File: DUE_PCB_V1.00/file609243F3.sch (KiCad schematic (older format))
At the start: 13 parts, among them J26 Cutter, J27 MotorR, J28 MotorL, J32 24V In, U1 MC33926, U2 MC33926

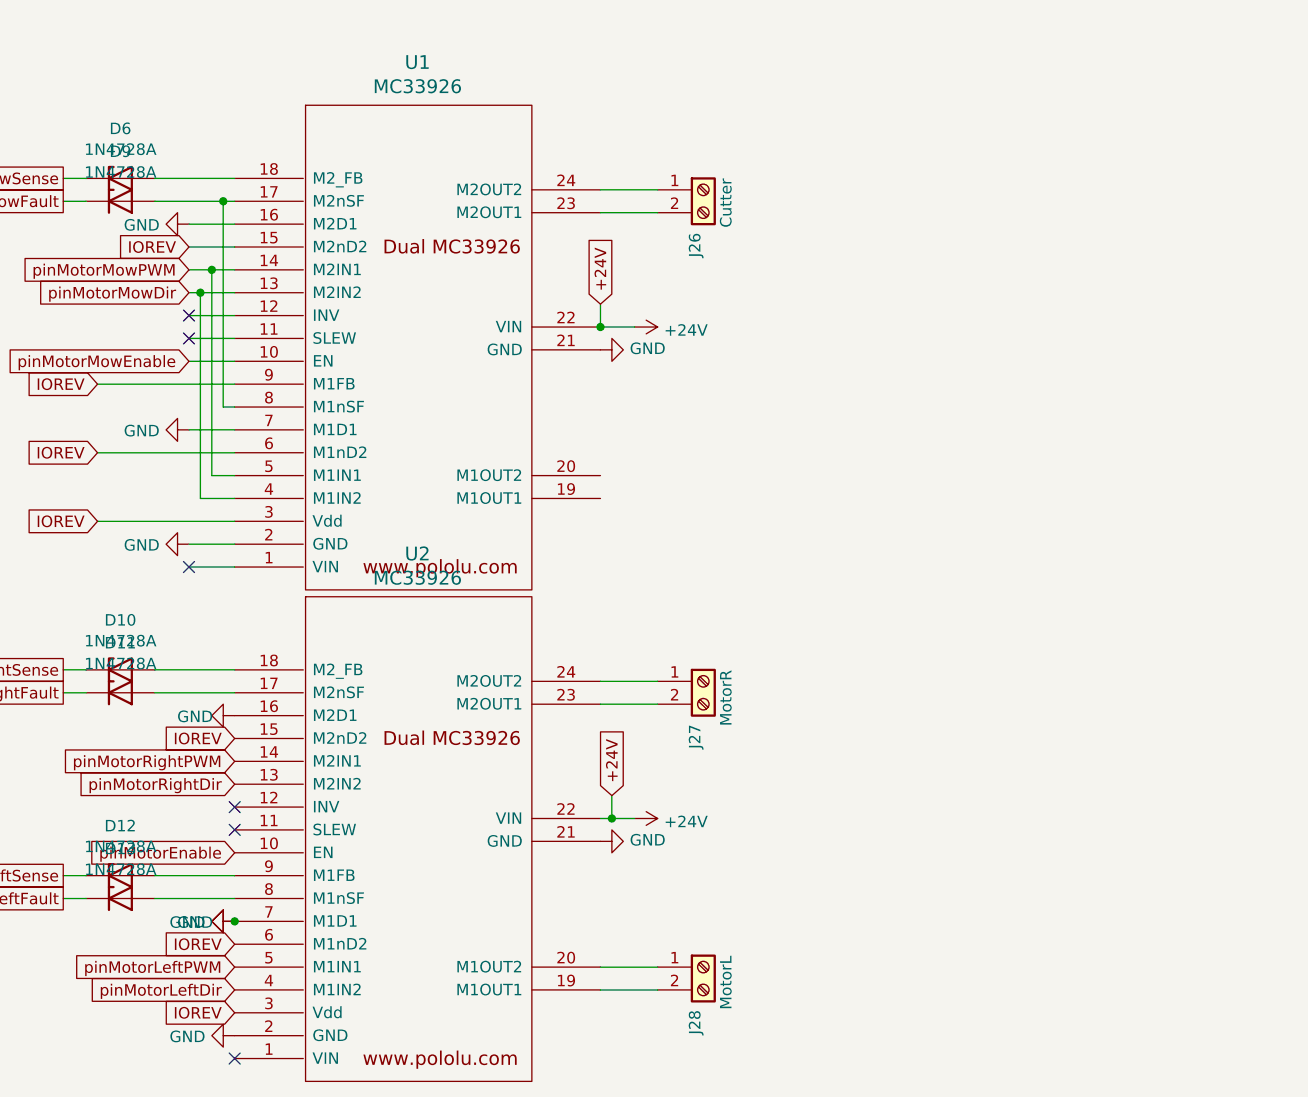
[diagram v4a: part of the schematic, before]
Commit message: Ad Odometrie Connector without Voltage Divider
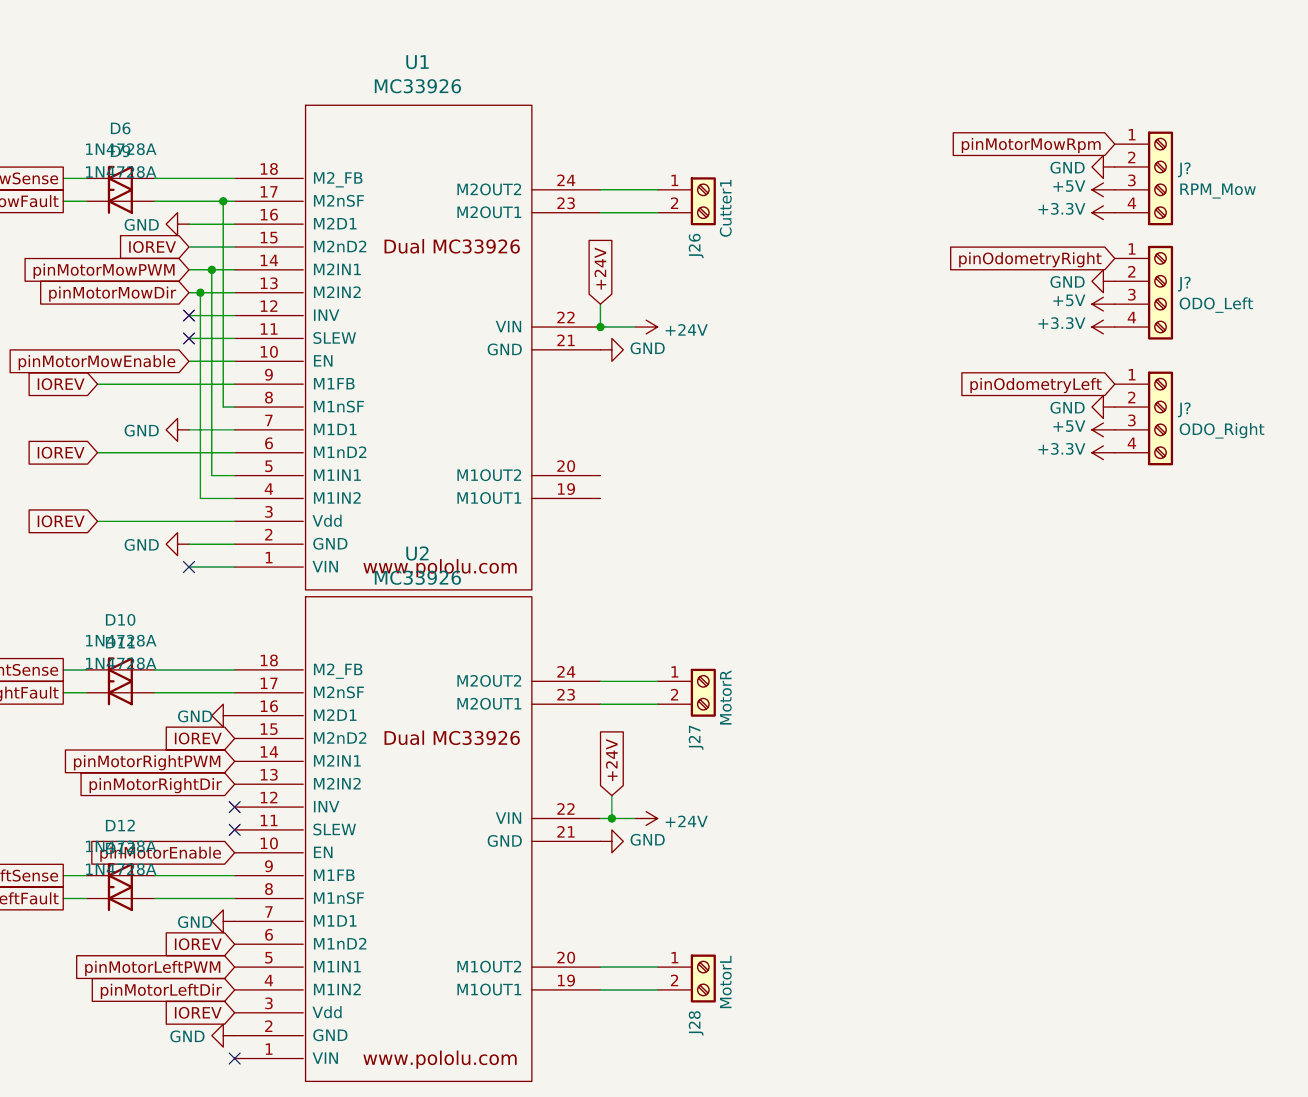
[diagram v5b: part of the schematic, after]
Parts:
- added J?: RPM_Mow, symbol Connector:Screw_Terminal_01x04
- added J?: ODO_Left, symbol Connector:Screw_Terminal_01x04
- added J?: ODO_Right, symbol Connector:Screw_Terminal_01x04
- J26: value Cutter -> Cutter1
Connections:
- net GND: now also J?.2 (Pin_2), J?.2 (Pin_2), J?.2 (Pin_2)
- new net +3V3: J?.4 (Pin_4), J?.4 (Pin_4), J?.4 (Pin_4)
- new net +5V: J?.3 (Pin_3), J?.3 (Pin_3), J?.3 (Pin_3)
- new net pinMotorMowRpm: J?.1 (Pin_1)
- new net pinOdometryLeft: J?.1 (Pin_1)
- new net pinOdometryRight: J?.1 (Pin_1)
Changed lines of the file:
@@
-$Comp
-L power:GND #PWR?
-U 1 1 60958CA1
-P 4300 4550
-AR Path="/60958CA1" Ref="#PWR?"  Part="1"
-AR Path="/609243F4/60958CA1" Ref="#PWR057"  Part="1"
-F 0 "#PWR057" H 4300 4300 50  0001 C CNN
-F 1 "GND" V 4305 4422 50  0000 R CNN
-F 2 "" H 4300 4550 50  0001 C CNN
-F 3 "" H 4300 4550 50  0001 C CNN
-	1    4300 4550
-	0    1    1    0
-$EndComp
 $Comp
 L power:GND #PWR?
@@
 P 6350 1350
 F 0 "J26" V 6314 1162 50  0000 R CNN
-F 1 "Cutter" V 6450 1400 50  0000 R CNN
+F 1 "Cutter1" V 6450 1400 50  0000 R CNN
 F 2 "TerminalBlock:TerminalBlock_bornier-2_P5.08mm" H 6350 1350 50  0001 C CNN
 F 3 "~" H 6350 1350 50  0001 C CNN
@@
 Wire Wire Line
 	3950 4450 4300 4450
-Connection ~ 4300 4550
+$Comp
+L Connector:Screw_Terminal_01x04 J?
+U 1 1 609ECE3C
+P 8350 1250
+F 0 "J?" H 8430 1242 50  0000 L CNN
+F 1 "RPM_Mow" H 8430 1151 50  0000 L CNN
+F 2 "" H 8350 1250 50  0001 C CNN
+F 3 "~" H 8350 1250 50  0001 C CNN
+	1    8350 1250
+	1    0    0    -1
+$EndComp
+$Comp
+L power:+3.3V #PWR?
+U 1 1 609FEF3C
+P 8150 1450
+F 0 "#PWR?" H 8150 1300 50  0001 C CNN
+F 1 "+3.3V" V 8165 1578 50  0000 L CNN
+F 2 "" H 8150 1450 50  0001 C CNN
+F 3 "" H 8150 1450 50  0001 C CNN
+	1    8150 1450
+	0    -1   -1   0
+$EndComp
+$Comp
+L power:+5V #PWR?
+U 1 1 60A02069
+P 8150 1350
+F 0 "#PWR?" H 8150 1200 50  0001 C CNN
+F 1 "+5V" V 8165 1478 50  0000 L CNN
+F 2 "" H 8150 1350 50  0001 C CNN
+F 3 "" H 8150 1350 50  0001 C CNN
+	1    8150 1350
+	0    -1   -1   0
+$EndComp
+$Comp
+L power:GND #PWR?
+U 1 1 60A04DCE
+P 8150 1250
+F 0 "#PWR?" H 8150 1000 50  0001 C CNN
+F 1 "GND" V 8155 1122 50  0000 R CNN
+F 2 "" H 8150 1250 50  0001 C CNN
+F 3 "" H 8150 1250 50  0001 C CNN
+	1    8150 1250
+	0    1    1    0
+$EndComp
+Text GLabel 8150 1150 0    50   Input ~ 0
+pinMotorMowRpm
+$Comp
+L Connector:Screw_Terminal_01x04 J?
+U 1 1 60A0AEEA
+P 8350 1750
+F 0 "J?" H 8430 1742 50  0000 L CNN
+F 1 "ODO_Left" H 8430 1651 50  0000 L CNN
+F 2 "" H 8350 1750 50  0001 C CNN
+F 3 "~" H 8350 1750 50  0001 C CNN
+	1    8350 1750
+	1    0    0    -1
+$EndComp
+$Comp
+L power:+3.3V #PWR?
+U 1 1 60A0B19C
+P 8150 1950
+F 0 "#PWR?" H 8150 1800 50  0001 C CNN
+F 1 "+3.3V" V 8165 2078 50  0000 L CNN
+F 2 "" H 8150 1950 50  0001 C CNN
+F 3 "" H 8150 1950 50  0001 C CNN
+	1    8150 1950
+	0    -1   -1   0
+$EndComp
+$Comp
+L power:+5V #PWR?
+U 1 1 60A0B1A6
+P 8150 1850
+F 0 "#PWR?" H 8150 1700 50  0001 C CNN
+F 1 "+5V" V 8165 1978 50  0000 L CNN
+F 2 "" H 8150 1850 50  0001 C CNN
+F 3 "" H 8150 1850 50  0001 C CNN
+	1    8150 1850
+	0    -1   -1   0
+$EndComp
+$Comp
+L power:GND #PWR?
+U 1 1 60A0B1B0
+P 8150 1750
+F 0 "#PWR?" H 8150 1500 50  0001 C CNN
+F 1 "GND" V 8155 1622 50  0000 R CNN
+F 2 "" H 8150 1750 50  0001 C CNN
+F 3 "" H 8150 1750 50  0001 C CNN
+	1    8150 1750
+	0    1    1    0
+$EndComp
+Text GLabel 8150 1650 0    50   Input ~ 0
+pinOdometryRight
+$Comp
+L Connector:Screw_Terminal_01x04 J?
+U 1 1 60A0D0C7
+P 8350 2300
+F 0 "J?" H 8430 2292 50  0000 L CNN
+F 1 "ODO_Right" H 8430 2201 50  0000 L CNN
+F 2 "" H 8350 2300 50  0001 C CNN
+F 3 "~" H 8350 2300 50  0001 C CNN
+	1    8350 2300
+	1    0    0    -1
+$EndComp
+$Comp
+L power:+3.3V #PWR?
+U 1 1 60A0D3D3
+P 8150 2500
+F 0 "#PWR?" H 8150 2350 50  0001 C CNN
+F 1 "+3.3V" V 8165 2628 50  0000 L CNN
+F 2 "" H 8150 2500 50  0001 C CNN
+F 3 "" H 8150 2500 50  0001 C CNN
+	1    8150 2500
+	0    -1   -1   0
+$EndComp
+$Comp
+L power:+5V #PWR?
+U 1 1 60A0D3DD
+P 8150 2400
+F 0 "#PWR?" H 8150 2250 50  0001 C CNN
+F 1 "+5V" V 8165 2528 50  0000 L CNN
+F 2 "" H 8150 2400 50  0001 C CNN
+F 3 "" H 8150 2400 50  0001 C CNN
+	1    8150 2400
+	0    -1   -1   0
+$EndComp
+$Comp
+L power:GND #PWR?
+U 1 1 60A0D3E7
+P 8150 2300
+F 0 "#PWR?" H 8150 2050 50  0001 C CNN
+F 1 "GND" V 8155 2172 50  0000 R CNN
+F 2 "" H 8150 2300 50  0001 C CNN
+F 3 "" H 8150 2300 50  0001 C CNN
+	1    8150 2300
+	0    1    1    0
+$EndComp
+Text GLabel 8150 2200 0    50   Input ~ 0
+pinOdometryLeft
 $EndSCHEMATC

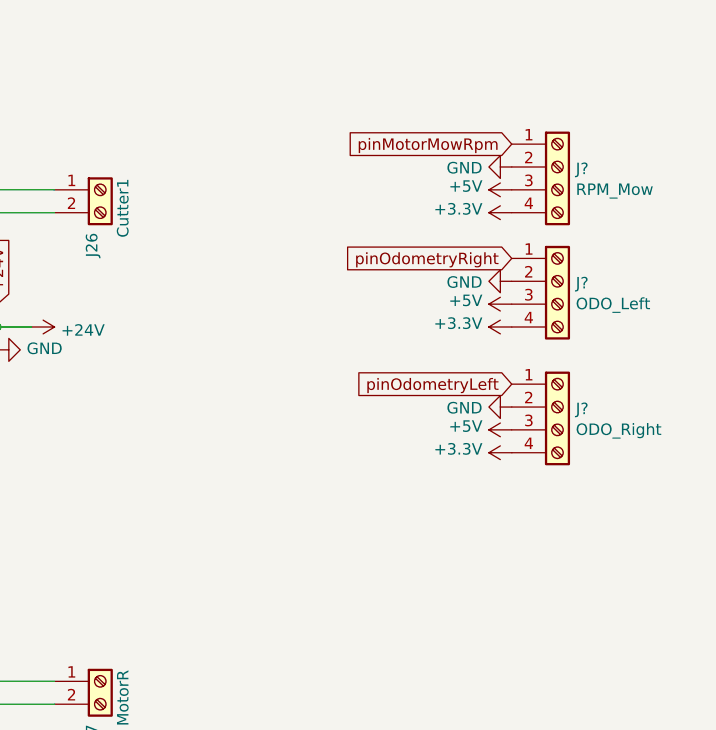
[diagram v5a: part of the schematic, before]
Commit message: Add Voltage Divider to ODO
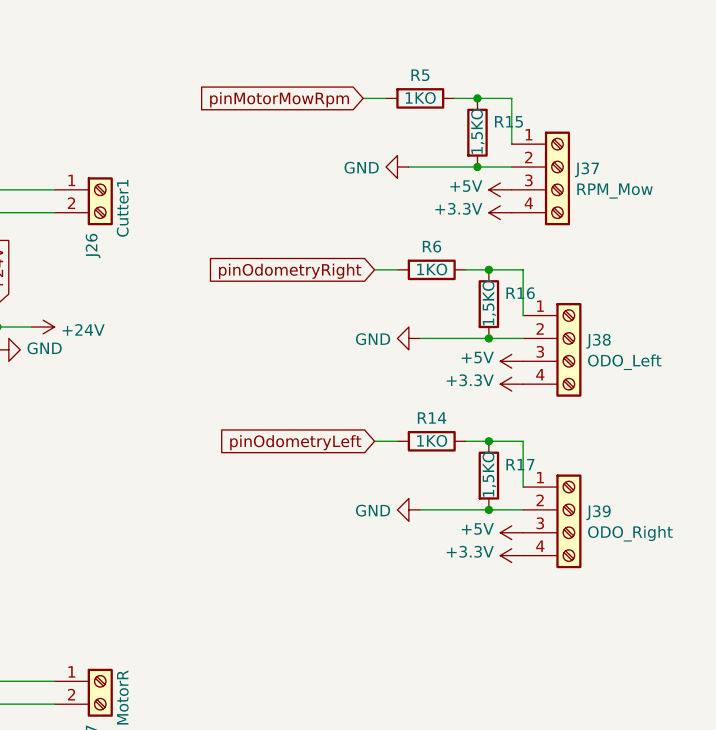
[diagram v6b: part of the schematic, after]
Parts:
- added R14, R5, R6: 1KO, Resistor_THT:R_Axial_DIN0207_L6.3mm_D2.5mm_P2.54mm_Vertical, symbol Device:R
- added R15, R16, R17: 1,5KO, Resistor_THT:R_Axial_DIN0207_L6.3mm_D2.5mm_P2.54mm_Vertical, symbol Device:R
- J37, J38, J39: renamed from J?; footprint (none) -> Connector_PinHeader_2.54mm:PinHeader_1x04_P2.54mm_Vertical
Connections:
- net GND: now also R15.2, R16.2, R17.2
- net pinMotorMowRpm: now also R5.2; no longer J37.1 (Pin_1)
- net pinOdometryLeft: now also R14.2; no longer J39.1 (Pin_1)
- net pinOdometryRight: now also R6.2; no longer J38.1 (Pin_1)
- new net: J37.1 (Pin_1), R15.1, R5.1
- new net: J38.1 (Pin_1), R16.1, R6.1
- new net: J39.1 (Pin_1), R14.1, R17.1
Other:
- moved on the sheet: J38, J39

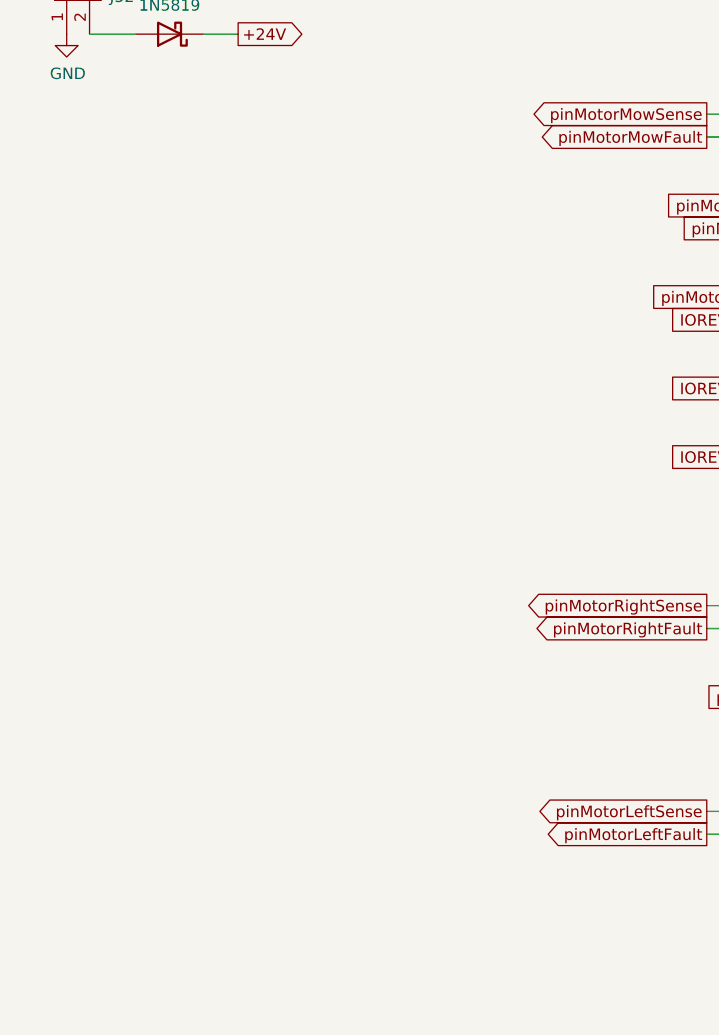
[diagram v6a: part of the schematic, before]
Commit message: Add Motor Connectors
Add Default Motor Connectors and reorder Ser0-Ser3
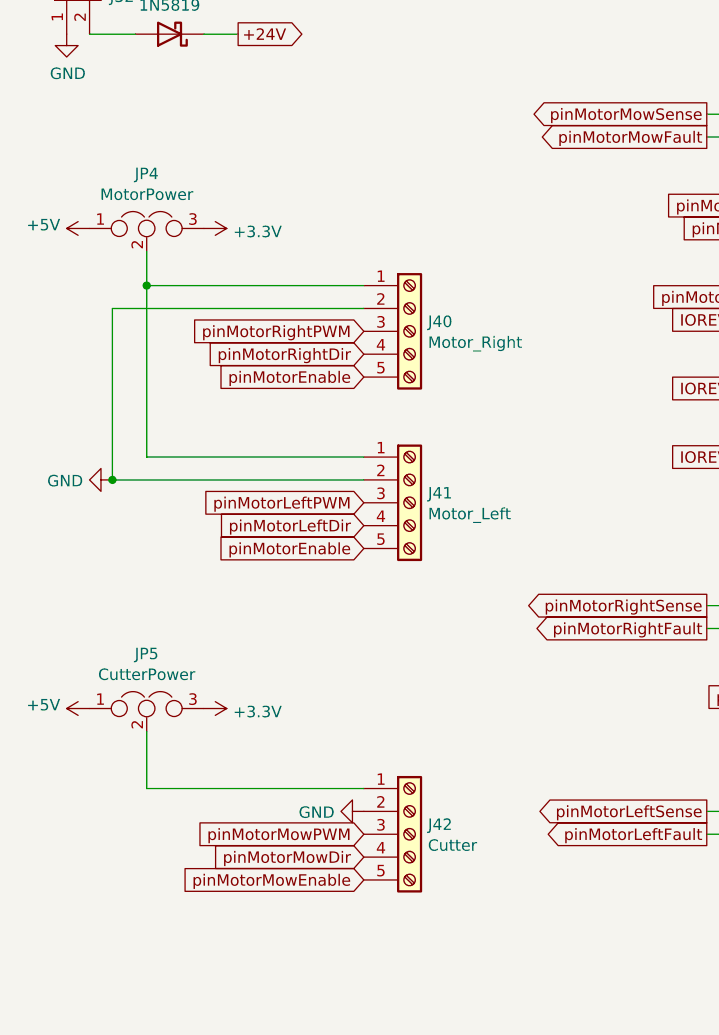
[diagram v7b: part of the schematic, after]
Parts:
- added J40: Motor_Right, Connector_PinSocket_2.54mm:PinSocket_1x05_P2.54mm_Vertical, symbol Connector:Screw_Terminal_01x05
- added J41: Motor_Left, Connector_PinSocket_2.54mm:PinSocket_1x05_P2.54mm_Vertical, symbol Connector:Screw_Terminal_01x05
- added J42: Cutter, Connector_PinSocket_2.54mm:PinSocket_1x05_P2.54mm_Vertical, symbol Connector:Screw_Terminal_01x05
- added JP4: MotorPower, Connector_PinSocket_2.54mm:PinSocket_1x03_P2.54mm_Vertical, symbol Device:Jumper_NC_Dual
- added JP5: CutterPower, Connector_PinSocket_2.54mm:PinSocket_1x03_P2.54mm_Vertical, symbol Device:Jumper_NC_Dual
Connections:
- net +3V3: now also JP4.3, JP5.3
- net +5V: now also JP4.1, JP5.1
- net GND: now also J40.2 (Pin_2), J41.2 (Pin_2), J42.2 (Pin_2)
- net pinMotorEnable: now also J40.5 (Pin_5), J41.5 (Pin_5)
- net pinMotorLeftDir: now also J41.4 (Pin_4)
- net pinMotorLeftPWM: now also J41.3 (Pin_3)
- net pinMotorMowDir: now also J42.4 (Pin_4)
- net pinMotorMowEnable: now also J42.5 (Pin_5)
- net pinMotorMowPWM: now also J42.3 (Pin_3)
- net pinMotorRightDir: now also J40.4 (Pin_4)
- net pinMotorRightPWM: now also J40.3 (Pin_3)
- new net: J40.1 (Pin_1), J41.1 (Pin_1), JP4.2
- new net: J42.1 (Pin_1), JP5.2
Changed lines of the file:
@@
 Wire Wire Line
 	8200 2450 8200 2650
+$Comp
+L Connector:Screw_Terminal_01x05 J40
+U 1 1 60A17AF1
+P 2250 2250
+F 0 "J40" H 2330 2292 50  0000 L CNN
+F 1 "Motor_Right" H 2330 2201 50  0000 L CNN
+F 2 "Connector_PinSocket_2.54mm:PinSocket_1x05_P2.54mm_Vertical" H 2250 2250 50  0001 C CNN
+F 3 "~" H 2250 2250 50  0001 C CNN
+	1    2250 2250
+	1    0    0    -1
+$EndComp
+$Comp
+L Device:Jumper_NC_Dual JP4
+U 1 1 60A196AB
+P 1100 1800
+F 0 "JP4" H 1100 2039 50  0000 C CNN
+F 1 "MotorPower" H 1100 1948 50  0000 C CNN
+F 2 "Connector_PinSocket_2.54mm:PinSocket_1x03_P2.54mm_Vertical" H 1100 1800 50  0001 C CNN
+F 3 "~" H 1100 1800 50  0001 C CNN
+	1    1100 1800
+	1    0    0    -1
+$EndComp
+$Comp
+L power:+3.3V #PWR092
+U 1 1 60A1A220
+P 1350 1800
+F 0 "#PWR092" H 1350 1650 50  0001 C CNN
+F 1 "+3.3V" V 1365 1928 50  0000 L CNN
+F 2 "" H 1350 1800 50  0001 C CNN
+F 3 "" H 1350 1800 50  0001 C CNN
+	1    1350 1800
+	0    1    1    0
+$EndComp
+$Comp
+L power:+5V #PWR089
+U 1 1 60A1A61A
+P 850 1800
+F 0 "#PWR089" H 850 1650 50  0001 C CNN
+F 1 "+5V" V 865 1928 50  0000 L CNN
+F 2 "" H 850 1800 50  0001 C CNN
+F 3 "" H 850 1800 50  0001 C CNN
+	1    850  1800
+	0    -1   -1   0
+$EndComp
+$Comp
+L power:GND #PWR091
+U 1 1 60A27474
+P 950 2900
+F 0 "#PWR091" H 950 2650 50  0001 C CNN
+F 1 "GND" V 955 2772 50  0000 R CNN
+F 2 "" H 950 2900 50  0001 C CNN
+F 3 "" H 950 2900 50  0001 C CNN
+	1    950  2900
+	0    1    1    0
+$EndComp
+Text GLabel 2050 2250 0    50   Input ~ 0
+pinMotorRightPWM
+Text GLabel 2050 2350 0    50   Input ~ 0
+pinMotorRightDir
+Text GLabel 2050 2450 0    50   Input ~ 0
+pinMotorEnable
+$Comp
+L Connector:Screw_Terminal_01x05 J41
+U 1 1 60A2B4C3
+P 2250 3000
+F 0 "J41" H 2330 3042 50  0000 L CNN
+F 1 "Motor_Left" H 2330 2951 50  0000 L CNN
+F 2 "Connector_PinSocket_2.54mm:PinSocket_1x05_P2.54mm_Vertical" H 2250 3000 50  0001 C CNN
+F 3 "~" H 2250 3000 50  0001 C CNN
+	1    2250 3000
+	1    0    0    -1
+$EndComp
+Text GLabel 2050 3000 0    50   Input ~ 0
+pinMotorLeftPWM
+Text GLabel 2050 3100 0    50   Input ~ 0
+pinMotorLeftDir
+Text GLabel 2050 3200 0    50   Input ~ 0
+pinMotorEnable
+$Comp
+L Connector:Screw_Terminal_01x05 J42
+U 1 1 60A3BF2F
+P 2250 4450
+F 0 "J42" H 2330 4492 50  0000 L CNN
+F 1 "Cutter" H 2330 4401 50  0000 L CNN
+F 2 "Connector_PinSocket_2.54mm:PinSocket_1x05_P2.54mm_Vertical" H 2250 4450 50  0001 C CNN
+F 3 "~" H 2250 4450 50  0001 C CNN
+	1    2250 4450
+	1    0    0    -1
+$EndComp
+Text GLabel 2050 4450 0    50   Input ~ 0
+pinMotorMowPWM
+Text GLabel 2050 4550 0    50   Input ~ 0
+pinMotorMowDir
+Text GLabel 2050 4650 0    50   Input ~ 0
+pinMotorMowEnable
+$Comp
+L Device:Jumper_NC_Dual JP5
+U 1 1 60A40CF2
+P 1100 3900
+F 0 "JP5" H 1100 4139 50  0000 C CNN
+F 1 "CutterPower" H 1100 4048 50  0000 C CNN
+F 2 "Connector_PinSocket_2.54mm:PinSocket_1x03_P2.54mm_Vertical" H 1100 3900 50  0001 C CNN
+F 3 "~" H 1100 3900 50  0001 C CNN
+	1    1100 3900
+	1    0    0    -1
+$EndComp
+$Comp
+L power:+3.3V #PWR093
+U 1 1 60A4118A
+P 1350 3900
+F 0 "#PWR093" H 1350 3750 50  0001 C CNN
+F 1 "+3.3V" V 1365 4028 50  0000 L CNN
+F 2 "" H 1350 3900 50  0001 C CNN
+F 3 "" H 1350 3900 50  0001 C CNN
+	1    1350 3900
+	0    1    1    0
+$EndComp
+$Comp
+L power:+5V #PWR090
+U 1 1 60A41194
+P 850 3900
+F 0 "#PWR090" H 850 3750 50  0001 C CNN
+F 1 "+5V" V 865 4028 50  0000 L CNN
+F 2 "" H 850 3900 50  0001 C CNN
+F 3 "" H 850 3900 50  0001 C CNN
+	1    850  3900
+	0    -1   -1   0
+$EndComp
+Wire Wire Line
+	1100 4000 1100 4250
+$Comp
+L power:GND #PWR094
+U 1 1 60A4A597
+P 2050 4350
+F 0 "#PWR094" H 2050 4100 50  0001 C CNN
+F 1 "GND" V 2055 4222 50  0000 R CNN
+F 2 "" H 2050 4350 50  0001 C CNN
+F 3 "" H 2050 4350 50  0001 C CNN
+	1    2050 4350
+	0    1    1    0
+$EndComp
+Wire Wire Line
+	1100 4250 2050 4250
+Wire Wire Line
+	2050 2050 1100 2050
+Wire Wire Line
+	1100 2050 1100 1900
+Wire Wire Line
+	2050 2800 1100 2800
+Wire Wire Line
+	1100 2800 1100 2050
+Connection ~ 1100 2050
+Wire Wire Line
+	2050 2150 950  2150
+Wire Wire Line
+	950  2150 950  2900
+Wire Wire Line
+	950  2900 2050 2900
+Connection ~ 950  2900
 $EndSCHEMATC
